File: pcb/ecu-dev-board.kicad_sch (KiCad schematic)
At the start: 2 parts, among them J1 MX23A18NF1, J2 39-30-1020

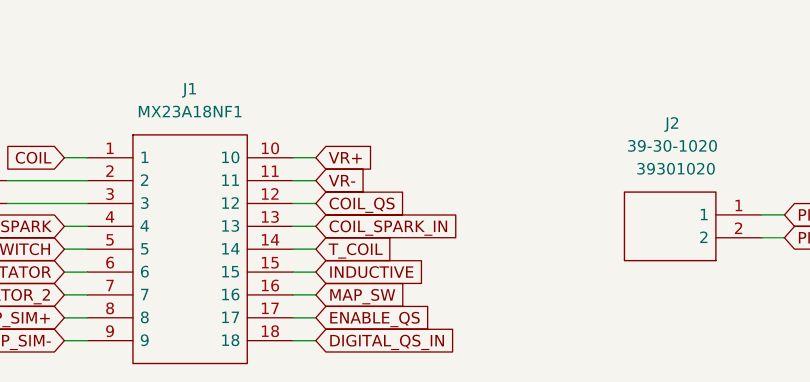
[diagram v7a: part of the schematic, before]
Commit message: MCU labels rework
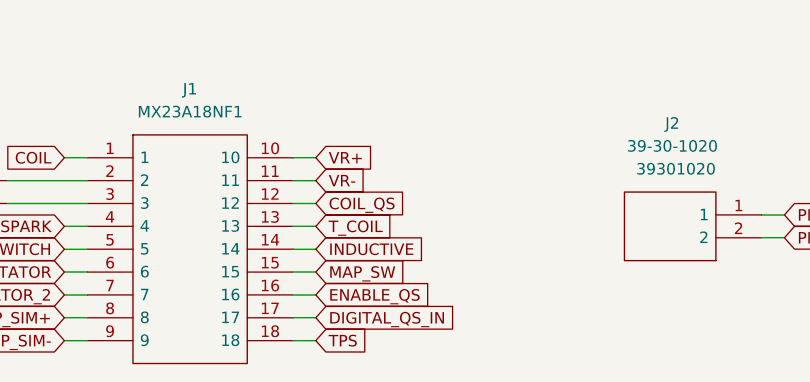
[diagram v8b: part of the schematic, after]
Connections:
- net COIL_SPARK_IN is gone; now on net T_COIL: J1.13
- net DIGITAL_QS_IN: now also J1.17; no longer J1.18
- net ENABLE_QS: now also J1.16; no longer J1.17
- net INDUCTIVE: now also J1.14; no longer J1.15
- net MAP_SW: now also J1.15; no longer J1.16
- net T_COIL: no longer J1.14
- new net TPS: J1.18
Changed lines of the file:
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@@
+		)
+	)
+	(global_label "ENABLE_QS"
+		(shape input)
+		(at 81.28 179.07 0)
+		(fields_autoplaced yes)
+		(effects
+			(font
+				(size 1.27 1.27)
+			)
+			(justify left)
+		)
+		(property "Intersheetrefs" "${INTERSHEET_REFS}"
+			(at 94.788 179.07 0)
+			(effects
+				(font
+					(size 1.27 1.27)
+				)
+				(justify left)
+				(hide yes)
+			)
+		)
+	)
+	(global_label "INDUCTIVE"
+		(shape input)
+		(at 81.28 173.99 0)
+		(fields_autoplaced yes)
+		(effects
+			(font
+				(size 1.27 1.27)
+			)
+			(justify left)
+		)
+		(property "Intersheetrefs" "${INTERSHEET_REFS}"
+			(at 93.881 173.99 0)
+			(effects
+				(font
+					(size 1.27 1.27)
+				)
+				(justify left)
+				(hide yes)
+			)
+		)
+	)
+	(global_label "VR+"
+		(shape input)
+		(at 81.28 163.83 0)
+		(fields_autoplaced yes)
+		(effects
+			(font
+				(size 1.27 1.27)
+			)
+			(justify left)
+		)
+		(property "Intersheetrefs" "${INTERSHEET_REFS}"
+			(at 88.1962 163.83 0)
+			(effects
+				(font
+					(size 1.27 1.27)
+				)
+				(justify left)
+				(hide yes)
+			)
+		)
+	)
+	(global_label "DIGITAL_QS_IN"
+		(shape input)
+		(at 81.28 181.61 0)
+		(fields_autoplaced yes)
+		(effects
+			(font
+				(size 1.27 1.27)
+			)
+			(justify left)
+		)
+		(property "Intersheetrefs" "${INTERSHEET_REFS}"
+			(at 97.5096 181.61 0)
+			(effects
+				(font
+					(size 1.27 1.27)
+				)
+				(justify left)
+				(hide yes)
+			)
+		)
+	)
+	(global_label "PIEZO+"
+		(shape input)
+		(at 133.35 170.18 0)
+		(fields_autoplaced yes)
+		(effects
+			(font
+				(size 1.27 1.27)
+			)
+			(justify left)
+		)
+		(property "Intersheetrefs" "${INTERSHEET_REFS}"
+			(at 143.4714 170.18 0)
+			(effects
+				(font
+					(size 1.27 1.27)
+				)
+				(justify left)
+				(hide yes)
+			)
 		)
 	)
 	(global_label "MAP_SW"
 		(shape input)
-		(at 81.28 179.07 0)
-		(fields_autoplaced yes)
-		(effects
-			(font
-				(size 1.27 1.27)
-			)
-			(justify left)
-		)
-		(property "Intersheetrefs" "${INTERSHEET_REFS}"
-			(at 91.7037 179.07 0)
-			(effects
-				(font
-					(size 1.27 1.27)
-				)
-				(justify left)
-				(hide yes)
-			)
-		)
-	)
-	(global_label "ENABLE_QS"
-		(shape input)
-		(at 81.28 181.61 0)
-		(fields_autoplaced yes)
-		(effects
-			(font
-				(size 1.27 1.27)
-			)
-			(justify left)
-		)
-		(property "Intersheetrefs" "${INTERSHEET_REFS}"
-			(at 94.788 181.61 0)
-			(effects
-				(font
-					(size 1.27 1.27)
-				)
-				(justify left)
-				(hide yes)
-			)
-		)
-	)
-	(global_label "VR+"
-		(shape input)
-		(at 81.28 163.83 0)
-		(fields_autoplaced yes)
-		(effects
-			(font
-				(size 1.27 1.27)
-			)
-			(justify left)
-		)
-		(property "Intersheetrefs" "${INTERSHEET_REFS}"
-			(at 88.1962 163.83 0)
-			(effects
-				(font
-					(size 1.27 1.27)
-				)
-				(justify left)
-				(hide yes)
-			)
-		)
-	)
-	(global_label "PIEZO+"
-		(shape input)
-		(at 133.35 170.18 0)
-		(fields_autoplaced yes)
-		(effects
-			(font
-				(size 1.27 1.27)
-			)
-			(justify left)
-		)
-		(property "Intersheetrefs" "${INTERSHEET_REFS}"
-			(at 143.4714 170.18 0)
-			(effects
-				(font
-					(size 1.27 1.27)
-				)
-				(justify left)
-				(hide yes)
-			)
-		)
-	)
-	(global_label "INDUCTIVE"
-		(shape input)
 		(at 81.28 176.53 0)
 		(fields_autoplaced yes)
@@
 		)
 		(property "Intersheetrefs" "${INTERSHEET_REFS}"
-			(at 93.881 176.53 0)
+			(at 91.7037 176.53 0)
 			(effects
 				(font
@@
 		)
 	)
+	(global_label "TPS"
+		(shape input)
+		(at 81.28 184.15 0)
+		(fields_autoplaced yes)
+		(effects
+			(font
+				(size 1.27 1.27)
+			)
+			(justify left)
+		)
+		(property "Intersheetrefs" "${INTERSHEET_REFS}"
+			(at 87.7123 184.15 0)
+			(effects
+				(font
+					(size 1.27 1.27)
+				)
+				(justify left)
+				(hide yes)
+			)
+		)
+	)
+	(global_label "COIL"
+		(shape input)
+		(at 53.34 163.83 180)
+		(fields_autoplaced yes)
+		(effects
+			(font
+				(size 1.27 1.27)
+			)
+			(justify right)
+		)
+		(property "Intersheetrefs" "${INTERSHEET_REFS}"
+			(at 46.1214 163.83 0)
+			(effects
+				(font
+					(size 1.27 1.27)
+				)
+				(justify right)
+				(hide yes)
+			)
+		)
+	)
 	(global_label "T_COIL"
 		(shape input)
-		(at 81.28 173.99 0)
-		(fields_autoplaced yes)
-		(effects
-			(font
-				(size 1.27 1.27)
-			)
-			(justify left)
-		)
-		(property "Intersheetrefs" "${INTERSHEET_REFS}"
-			(at 90.4338 173.99 0)
-			(effects
-				(font
-					(size 1.27 1.27)
-				)
-				(justify left)
-				(hide yes)
-			)
-		)
-	)
-	(global_label "COIL_SPARK_IN"
-		(shape input)
 		(at 81.28 171.45 0)
 		(fields_autoplaced yes)
@@
 		)
 		(property "Intersheetrefs" "${INTERSHEET_REFS}"
-			(at 98.4772 171.45 0)
-			(effects
-				(font
-					(size 1.27 1.27)
-				)
-				(justify left)
-				(hide yes)
-			)
-		)
-	)
-	(global_label "COIL"
-		(shape input)
-		(at 53.34 163.83 180)
-		(fields_autoplaced yes)
-		(effects
-			(font
-				(size 1.27 1.27)
-			)
-			(justify right)
-		)
-		(property "Intersheetrefs" "${INTERSHEET_REFS}"
-			(at 46.1214 163.83 0)
-			(effects
-				(font
-					(size 1.27 1.27)
-				)
-				(justify right)
-				(hide yes)
-			)
-		)
-	)
-	(global_label "DIGITAL_QS_IN"
-		(shape input)
-		(at 81.28 184.15 0)
-		(fields_autoplaced yes)
-		(effects
-			(font
-				(size 1.27 1.27)
-			)
-			(justify left)
-		)
-		(property "Intersheetrefs" "${INTERSHEET_REFS}"
-			(at 97.5096 184.15 0)
-			(effects
-				(font
+			(at 90.4338 171.45 0)
+			(effects
+				(font
